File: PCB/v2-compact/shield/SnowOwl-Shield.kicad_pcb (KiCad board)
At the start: 4 copper layers, 70 x 100 mm, 80 parts, among them J1 STACK_2x10, J40 C5_PROG_UART, J50 USB-C, J51 microSD, J91 iButton, Q1 MMBT3904, U1 nRF24L01+, U11 TSOP38238, U12 W25Q128JVSSIQ, U2 nRF24L01+, U3 nRF24L01+, U4 CC1101, U40 ESP32-C5-WROOM-1U-N16R4, U41 AP7361C-3.3, U42 MCP23S17, U5 CC1200RHBR, U6 SX1262IMLTRT, U7 PN532, U8 HTRC11001T, U9 NEO-M9N, Y50 27.12MHz, Y60 40MHz, Y61 32MHz, Y90 4MHz

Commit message: PCB: place the missing RV1106, keep parts in their floorplan zones
Placement audit pass (every netlist part on the board + each near its zone) found and fixed:
- U30 (RV1106 SoM, a MAIN IC) was NOT on the board: it's the only part with an empty
  footprint field in the netlist, so the importer silently skipped it. Added it with the
  on-disk RV1106_Core1106 placeholder footprint, assigned its 14 nets, placed it in the
  RV1106 zone on the back with J50/J51 nudged clear of it.
- 4 RV1106 decoupling parts (C94/C95/R95/R96) had wandered ~40mm to the GPS/radio band.
  Two causes: (a) U30's absence left them no zone anchor; (b) they share the CC12_DCPL
  net (see below) which spans the board. Fixed by constraining the anchoring to a part's
  own zone (reject a shared-net anchor >24mm from the sheet), and adding CC12_DCPL to the
  rail-net set so it can't drag parts around.
- Harden the netlist parser's block extractor to ignore parens inside quoted strings.

Both boards re-verified: every part placed and in its zone, 0 overlaps, 0 cross-side hole
collisions, 0 parts too close to a mounting hole, nothing off the outline.

KNOWN ISSUES for the schematic (do NOT block placement, but must fix before routing):
1. NET BUG: GND has 0 nodes - every ground is merged into CC12_DCPL (99 nodes). Confirmed
   by KiCad's own netlister on a fresh export. A GND/CC12_DCPL short in the sub-GHz sheet.
2. U30 needs its footprint assigned in the schematic (currently added straight to the PCB).
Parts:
- added U30: Core1106_RV1106, RV1106_Core1106, B.Cu at (70.0, 84.0)
- C94, C95, R95, R96: moved to B.Cu
- moved C94 54.5 mm to (52.0, 97.0), turned to 180 degrees
- moved C95 51.2 mm to (49.3, 93.2), turned to 180 degrees
- moved R95 46.2 mm to (51.9, 93.1), turned to 180 degrees
- moved C61 26.8 mm to (53.4, 53.9)
- moved C62 24.2 mm to (56.3, 66.9)
- moved C70 20.9 mm to (92.9, 41.0)
- moved R57 20.1 mm to (48.8, 96.5)
- moved C72 16.8 mm to (76.1, 36.8)
- moved R96 16.3 mm to (89.1, 71.3), turned to 180 degrees
- moved C54 14.6 mm to (43.6, 68.5)
- moved C91 14.4 mm to (37.8, 87.5)
- moved C84 14.2 mm to (68.2, 38.2)
- moved C71 14.2 mm to (92.8, 39.6)
- moved C85 13.8 mm to (66.3, 44.7)
- moved R80 12.0 mm to (59.6, 47.2)
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
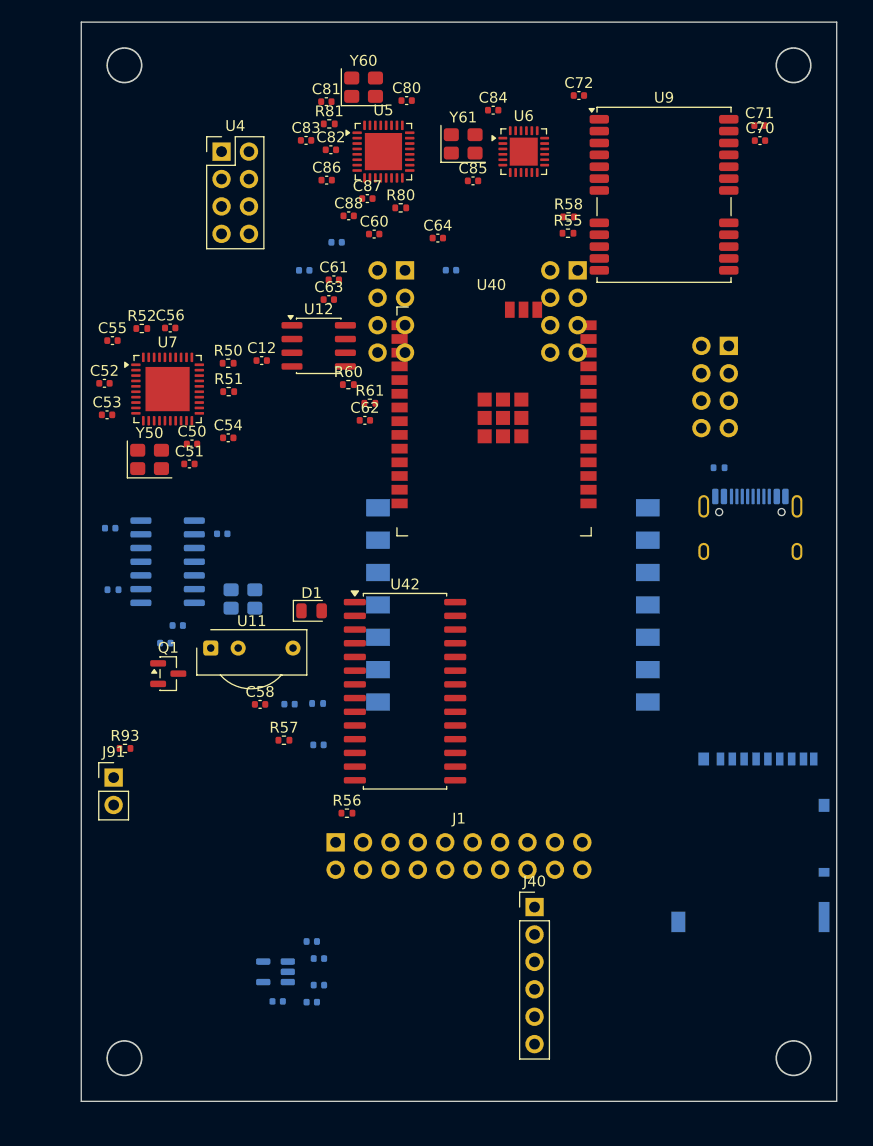
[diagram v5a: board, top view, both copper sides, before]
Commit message: PCB: orient microSD slots to the board edge, USB-C to the bottom-middle edge
Per the mechanical intent:
- microSD (J30 main, J51 shield): rotate to rot270 so the CARD SLOT opening faces the
  outside EAST edge - a card now slots straight in from the board edge instead of the slot
  pointing inward. Positioned so the opening sits at the edge.
- J50 (shield RV1106 USB-C): moved to the bottom-middle on the board edge with the opening
  facing SOUTH, matching J20 on the main board, so it's the charge + power/data port.
- Verified both USB-C receptacles carry power AND data: J20 = +5V/GND + USB_DP/DM + CC1/CC2;
  J50 = RV_5V + RV_USB_DP/DM + CC1/CC2.

Both boards still pass every check (0 overlaps, 0 cross-side hole collisions, 0 parts too
close to a mounting hole); the only edge flags are these connectors, which belong at the edge.
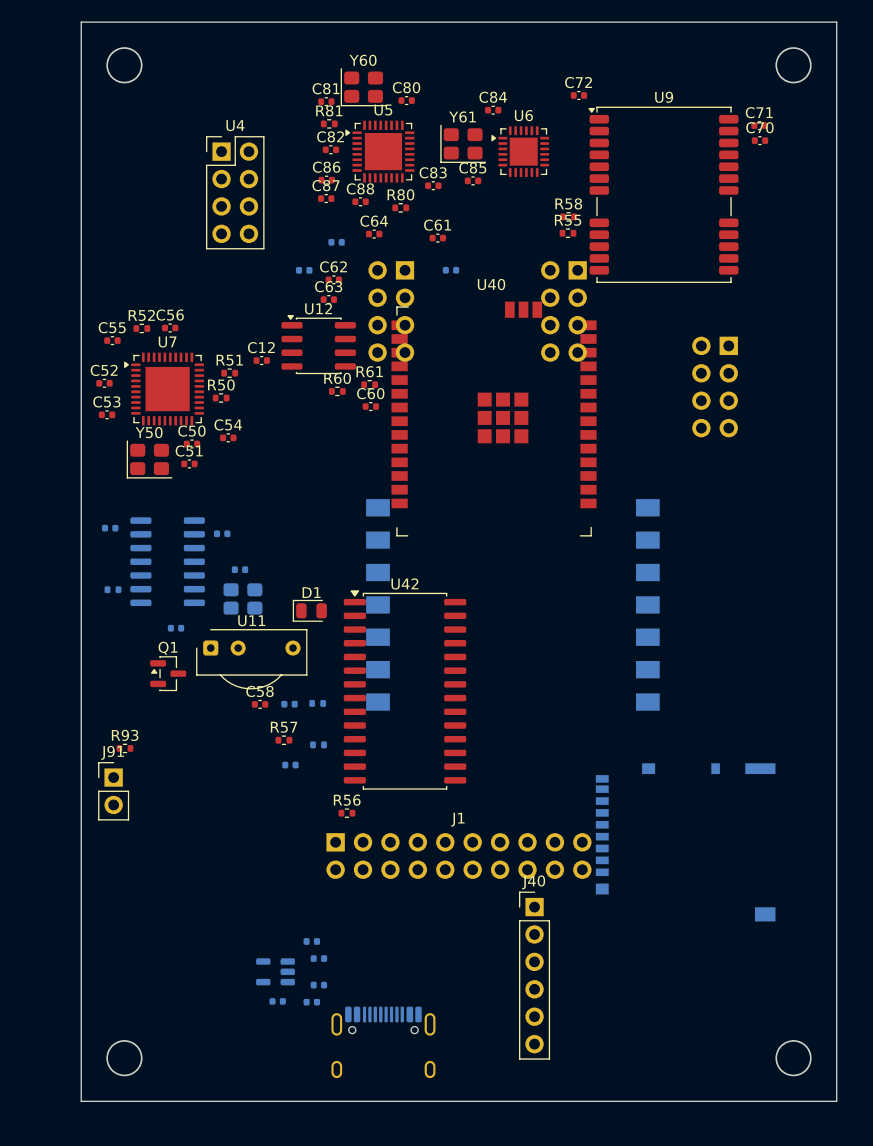
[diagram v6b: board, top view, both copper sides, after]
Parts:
- moved J50 58.8 mm to (58.0, 126.0)
- moved R96 43.1 mm to (51.9, 93.1)
- moved C60 16.0 mm to (56.8, 65.6)
- moved C62 13.3 mm to (53.4, 53.9)
- moved C83 12.5 mm to (62.6, 45.2)
- moved C61 10.4 mm to (63.0, 50.0)
- moved C90 7.75 mm to (44.7, 80.7)
- moved J51 6.00 mm to (86.0, 106.0), turned to -90 degrees
- moved C64 5.91 mm to (57.1, 49.6)
- moved C95 5.64 mm to (49.4, 98.8)
- moved C94 4.63 mm to (49.3, 93.2)
- moved R95 3.84 mm to (52.0, 97.0)
- moved C87 3.81 mm to (52.7, 46.4)
- moved R50 3.28 mm to (43.0, 64.8)
- moved R61 1.72 mm to (56.7, 63.6)
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
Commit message: Schematic: fix the GND<->CC12_DCPL short (empty ground net) + re-import nets
Root cause of GND having ZERO nodes: in the sub-GHz sheet, C82(+3V3/GND) & C83(CC12_DCPL/GND)
and C86(+3V3/GND) & C87(SX1262_VREG/GND) were each stacked exactly 12mm apart in the same
column. connect()'s 5.08mm wire stubs from the upper cap's GND pin snapped onto the lower
cap's non-GND pin, shorting GND to CC12_DCPL and to SX1262_VREG - which merged every ground
on the board into CC12_DCPL. Moved C83 and C87 off-column to clear positions.

- Verified by KiCad's netlister: GND now 64 comps (shield) / 25 (main), was 0; CC12_DCPL
  back to 2 nodes, SX1262_VREG back to 2.
- Regenerated all sheets, re-exported both netlists, and re-imported the corrected nets onto
  both .kicad_pcb (positions/footprints untouched): shield 433 pad-nets, main 150.
- Hardened the netlist parser's block extractor to skip parens inside quoted strings.
- Also confirmed the regen assigns U30's RV1106 footprint (the earlier empty-footprint netlist
  that made U30 vanish on import was stale).

The ground net can now actually form a plane - unblocks routing. Placement re-verified clean
(0 overlaps, 0 cross-side hole collisions).
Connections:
- C10 pad 2: CC12_DCPL -> GND
- C12 pad 2: CC12_DCPL -> GND
- C20 pad 2: CC12_DCPL -> GND
- C30 pad 2: CC12_DCPL -> GND
- C40 pad 2: CC12_DCPL -> GND
- C41 pad 2: CC12_DCPL -> GND
- C42 pad 2: CC12_DCPL -> GND
- C43 pad 2: CC12_DCPL -> GND
- C44 pad 2: CC12_DCPL -> GND
- C50 pad 2: CC12_DCPL -> GND
- C51 pad 2: CC12_DCPL -> GND
- C52 pad 2: CC12_DCPL -> GND
- C53 pad 2: CC12_DCPL -> GND
- C54 pad 2: CC12_DCPL -> GND
- C55 pad 2: CC12_DCPL -> GND
- C56 pad 2: CC12_DCPL -> GND
- C58 pad 2: CC12_DCPL -> GND
- C60 pad 2: CC12_DCPL -> GND
- C61 pad 2: CC12_DCPL -> GND
- C62 pad 2: CC12_DCPL -> GND
- C63 pad 2: CC12_DCPL -> GND
- C64 pad 2: CC12_DCPL -> GND
- C70 pad 2: CC12_DCPL -> GND
- C71 pad 2: CC12_DCPL -> GND
- C72 pad 2: CC12_DCPL -> GND
- C80 pad 2: CC12_DCPL -> GND
- C81 pad 2: CC12_DCPL -> GND
- C82 pad 2: CC12_DCPL -> GND
- C83 pad 2: CC12_DCPL -> GND
- C84 pad 2: CC12_DCPL -> GND
- C85 pad 2: CC12_DCPL -> GND
- C86 pad 2: CC12_DCPL -> GND
- C87 pad 1: CC12_DCPL -> SX1262_VREG
- C87 pad 2: CC12_DCPL -> GND
- C88 pad 2: CC12_DCPL -> GND
- C90 pad 2: CC12_DCPL -> GND
- C91 pad 2: CC12_DCPL -> GND
- C92 pad 2: CC12_DCPL -> GND
- C93 pad 2: CC12_DCPL -> GND
- C94 pad 2: CC12_DCPL -> GND
- C95 pad 2: CC12_DCPL -> GND
- J1 pad 10: CC12_DCPL -> GND
- J1 pad 11: CC12_DCPL -> GND
- J1 pad 15: CC12_DCPL -> GND
- J1 pad 20: CC12_DCPL -> GND
- J1 pad 3: CC12_DCPL -> GND
- J1 pad 6: CC12_DCPL -> GND
- J40 pad 2: CC12_DCPL -> GND
- J50 pad A1: CC12_DCPL -> GND
- J50 pad A12: CC12_DCPL -> GND
- J50 pad B1: CC12_DCPL -> GND
- J50 pad B12: CC12_DCPL -> GND
- J50 pad SH: CC12_DCPL -> GND
- J51 pad 6: CC12_DCPL -> GND
- J51 pad SH: CC12_DCPL -> GND
- J91 pad 2: CC12_DCPL -> GND
- Q1 pad 3: CC12_DCPL -> GND
- R80 pad 2: CC12_DCPL -> GND
- R95 pad 2: CC12_DCPL -> GND
- R96 pad 2: CC12_DCPL -> GND
- U1 pad 1: CC12_DCPL -> GND
- U11 pad 1: CC12_DCPL -> GND
- U12 pad 4: CC12_DCPL -> GND
- U2 pad 1: CC12_DCPL -> GND
- U3 pad 1: CC12_DCPL -> GND
- U30 pad 14: CC12_DCPL -> GND
- U4 pad 1: CC12_DCPL -> GND
- U40 pad 1: CC12_DCPL -> GND
- U40 pad 28: CC12_DCPL -> GND
- U40 pad 29: CC12_DCPL -> GND
- U40 pad 30: CC12_DCPL -> GND
- U40 pad 32: CC12_DCPL -> GND
- U41 pad 2: CC12_DCPL -> GND
- U42 pad 10: CC12_DCPL -> GND
- U42 pad 15: CC12_DCPL -> GND
- U42 pad 16: CC12_DCPL -> GND
- U42 pad 17: CC12_DCPL -> GND
- U5 pad 32: CC12_DCPL -> GND
- U5 pad 33: CC12_DCPL -> GND
- U6 pad 2: CC12_DCPL -> GND
- U6 pad 20: CC12_DCPL -> GND
- U6 pad 25: CC12_DCPL -> GND
- U6 pad 5: CC12_DCPL -> GND
- U6 pad 7: CC12_DCPL -> SX1262_VREG
- U6 pad 8: CC12_DCPL -> GND
- U7 pad 1: CC12_DCPL -> GND
- U7 pad 11: CC12_DCPL -> GND
- U7 pad 17: CC12_DCPL -> GND
- U7 pad 3: CC12_DCPL -> GND
- U7 pad 41: CC12_DCPL -> GND
- U7 pad 7: CC12_DCPL -> GND
- U8 pad 1: CC12_DCPL -> GND
- U8 pad 12: CC12_DCPL -> GND
- U9 pad 10: CC12_DCPL -> GND
- U9 pad 12: CC12_DCPL -> GND
- U9 pad 13: CC12_DCPL -> GND
- U9 pad 24: CC12_DCPL -> GND
